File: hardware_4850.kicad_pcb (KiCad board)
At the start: 4 copper layers, 207.2 x 123 mm, 285 parts, among them J101 PWM, J102 ADC, J103 PWM, J104 ADC, J105 +, J106 A, J107 B, J108 C, J109 GND, J1101 HALL, J1102 PWM_EN, J1103 CAN_IN, J1104 CAN_Out, J501 Enable, J601 AIN, J602 USB_B_Mini, J701 MOT_TEMP, P1101 SWD, Q201 NCEP6080AG, Q202 NCEP6080AG, Q203 NCEP6080AG, Q204 NCEP6080AG, Q301 NCEP6080AG, Q302 NCEP6080AG, Q303 NCEP6080AG, Q304 NCEP6080AG, Q401 NCEP6080AG, Q402 NCEP6080AG, Q403 NCEP6080AG, Q404 NCEP6080AG, U1001 GS8632-MR, U1101 TCAN334, U1102 24LC04, U1103 AP2204K-5.0, U201 LM5109BMA, U202 INA240A1PWR, U301 LM5109BMA, U302 INA240A1PWR, U401 LM5109BMA, U402 INA240A1PWR, U501 LMR12010Y, U502 LM5008, U601 STM32F730R8Tx, U701 GS8632-MR, U801 GS8632-MR, U901 GS8632-MR, X601 SM44T

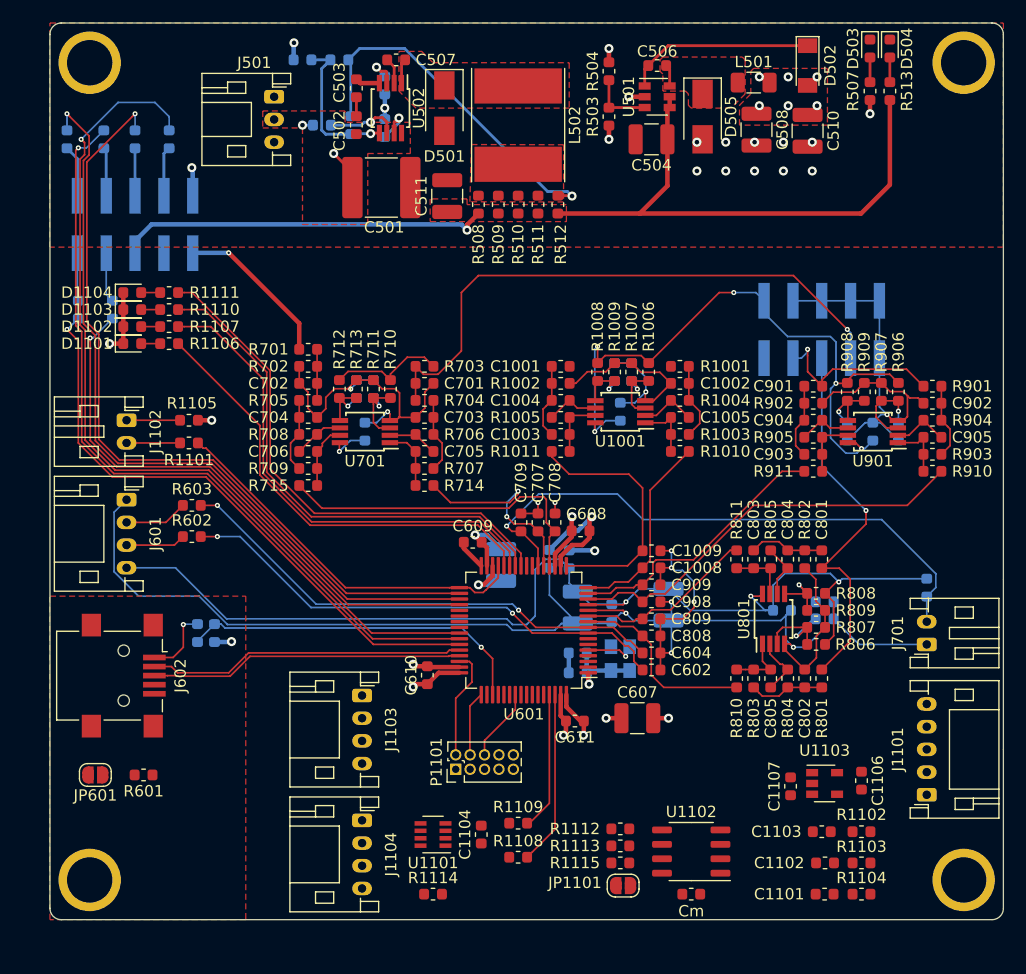
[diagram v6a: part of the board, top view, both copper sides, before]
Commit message: finished routing of logic pcb
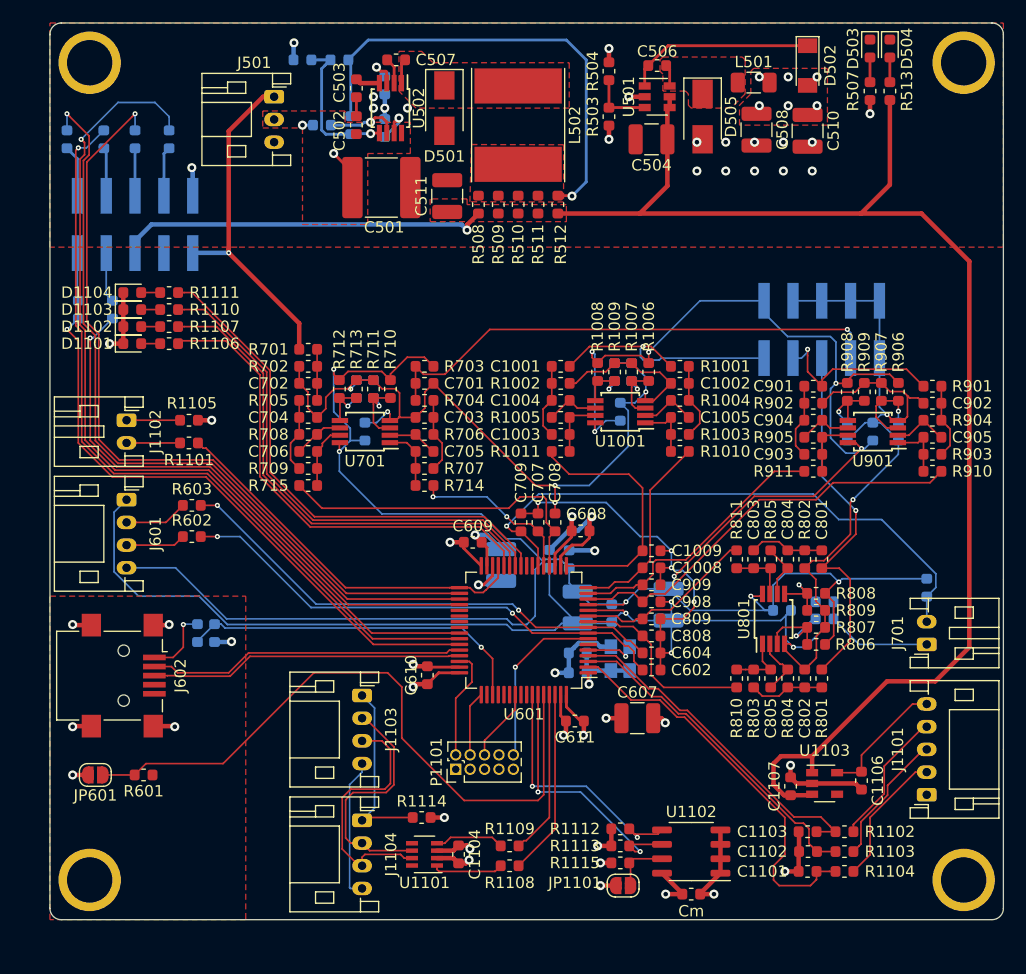
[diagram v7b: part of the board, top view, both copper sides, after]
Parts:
- moved R1114 6.82 mm to (213.0, 129.0)
- moved C1104 2.66 mm to (216.2, 132.2), turned to 270 degrees
- moved C1101 2.50 mm to (247.0, 133.8)
- moved R1104 2.50 mm to (250.2, 133.8)
- moved R1109 2.14 mm to (220.8, 131.5)
- moved U1101 1.90 mm to (213.2, 132.2)
- moved C1102 1.80 mm to (247.0, 132.0)
- moved R1103 1.80 mm to (250.2, 132.0)
- moved R1102 1.50 mm to (250.2, 130.2)
- moved C1103 1.25 mm to (247.0, 130.2)
- moved R1108 1.06 mm to (220.8, 133.2)
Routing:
- net +12V: track 82.2 -> 156.1 mm
- net /controller/BTLDR: track 0.00 -> 58.9 mm
- net GNDA: track 230.6 -> 287.3 mm, vias 13 -> 15
- net +3.3VADC: track 172.6 -> 225.4 mm, vias 9 -> 11
- net GNDD: track 46.2 -> 83.7 mm, vias 22 -> 36
- net /controller/interfaces/HallA: track 0.00 -> 35.3 mm
- net /controller/interfaces/HallC: track 0.00 -> 29.9 mm
- net /controller/interfaces/HallB: track 0.00 -> 29.5 mm
- net /controller/EEPROM_SDA: track 0.00 -> 23.9 mm, vias 0 -> 2
- net /controller/EEPROM_SCL: track 0.00 -> 23.5 mm, vias 0 -> 2
- net Net-(J1103-Pad3): track 0.00 -> 22.9 mm
- net /controller/Ic: track 0.00 -> 22.5 mm, vias 0 -> 1
- net Net-(J1103-Pad2): track 0.00 -> 21.7 mm
- net Net-(J1103-Pad1): track 0.00 -> 16.5 mm
- net +48V: track 14.3 -> 30.2 mm
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
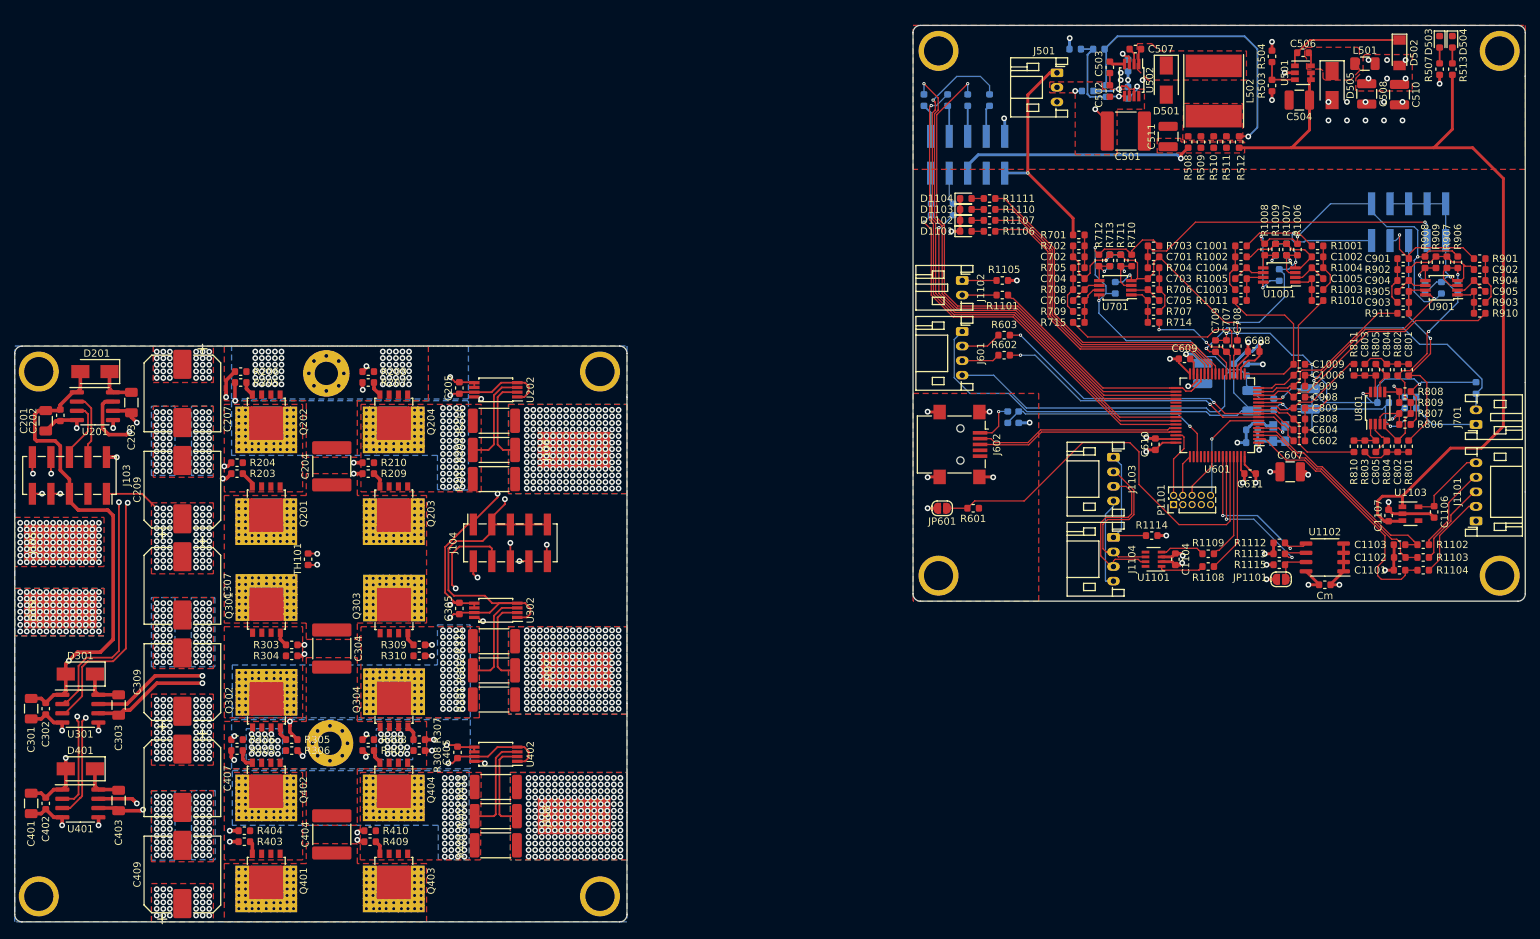
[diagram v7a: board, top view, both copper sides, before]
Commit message: made 3d design for mounting in enclosure
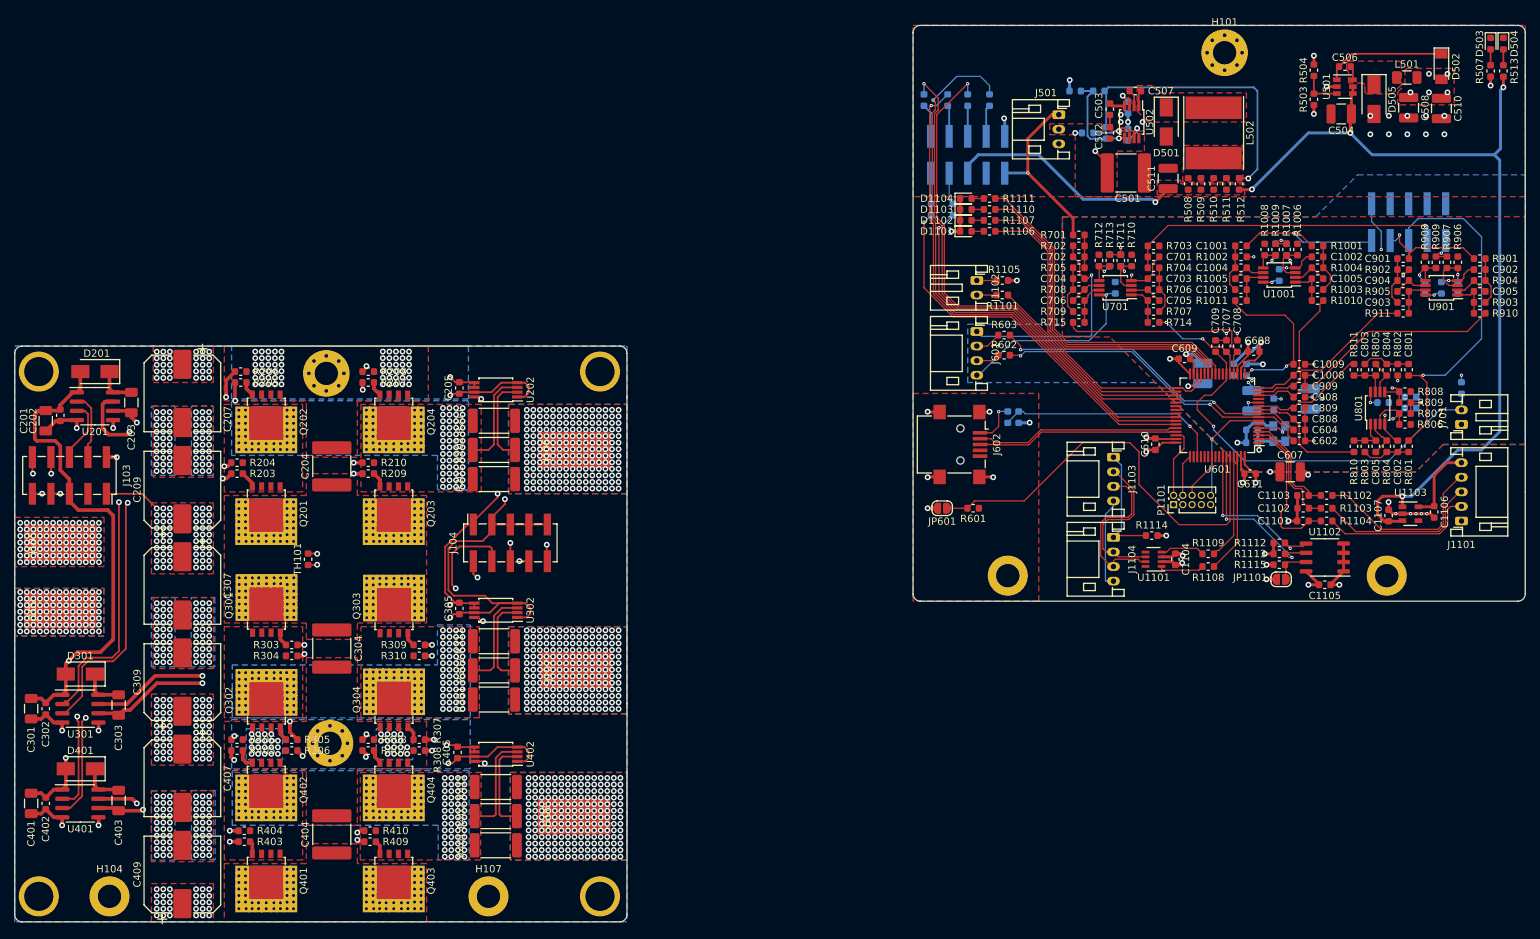
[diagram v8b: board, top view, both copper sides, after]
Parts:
- removed N102: Housing_Pad, hardware_4850:RND-455-00370
- added H101: GND, MountingHole:MountingHole_3.2mm_M3_Pad_Via, F.Cu at (223.0, 62.8)
- added H102: GND, MountingHole:MountingHole_3.2mm_M3_ISO14580_Pad, F.Cu at (193.2, 134.5)
- added H103: GND, MountingHole:MountingHole_3.2mm_M3_ISO14580_Pad, F.Cu at (245.2, 134.5)
- added H104: GND, MountingHole:MountingHole_3.2mm_M3_ISO14580_Pad, F.Cu at (70.0, 178.5)
- added H107: GND, MountingHole:MountingHole_3.2mm_M3_ISO14580_Pad, F.Cu at (122.0, 178.5)
- moved C1101 14.9 mm to (233.8, 127.0)
- moved C1102 14.9 mm to (233.8, 125.2)
- moved C1103 14.9 mm to (233.8, 123.5)
- moved R1102 14.9 mm to (237.0, 123.5)
- moved R1103 14.9 mm to (237.0, 125.2)
- moved R1104 14.9 mm to (237.0, 127.0)
- moved D503 7.00 mm to (259.5, 61.5)
- moved D504 7.00 mm to (261.2, 61.5)
- moved R507 7.00 mm to (259.5, 65.2)
- moved R513 7.00 mm to (261.2, 65.2)
- moved C504 6.06 mm to (239.0, 71.2)
- moved C506 6.06 mm to (239.5, 64.7)
- moved C510 6.06 mm to (252.8, 70.4)
- moved D502 6.06 mm to (252.8, 64.7)
- moved D505 6.06 mm to (243.5, 69.2)
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- renumbered Cm to C1105
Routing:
- net GNDA: track 287.3 -> 82.9 mm, vias 15 -> 19
- net +3.3VADC: track 225.4 -> 47.4 mm, vias 11 -> 10
- net /controller/Ia: track 32.9 -> 49.7 mm
- net /controller/interfaces/HallC: track 29.9 -> 14.8 mm
- net /controller/interfaces/HallA: track 35.3 -> 20.8 mm
- net /controller/interfaces/HallB: track 29.5 -> 15.9 mm
- net Net-(J1101-Pad4): track 12.1 -> 25.0 mm
- net Net-(J1101-Pad3): track 11.8 -> 22.8 mm
- net Net-(J1101-Pad2): track 12.0 -> 21.3 mm
- net +48V: track 30.2 -> 24.6 mm
- net /controller/analog/MotTemp: track 51.6 -> 55.4 mm
- net Net-(J601-Pad2): track 5.58 -> 3.58 mm
- net Net-(J1102-Pad2): track 4.71 -> 2.71 mm
- net Net-(J1102-Pad1): track 4.71 -> 2.71 mm
- net Net-(J601-Pad3): track 5.27 -> 3.27 mm
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- added copper zone on F.Cu, net +3.3VADC
- added copper zone on B.Cu, net GNDA
